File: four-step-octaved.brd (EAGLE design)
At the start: 93.7 x 43.2 mm, 36 parts, among them IC1 556, IC2 4017N, IC3 4040N, J1 BATTERY, J2 SPEAKER, U1 LM386N

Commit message: Routed
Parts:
- moved D2 0.63 mm to (5.08, 5.71)
- flipped C1 to the bottom
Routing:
- net GND: track 0.00 -> 250.5 mm
- net +9V: track 0.00 -> 132.8 mm
- net N$10: track 0.00 -> 79.7 mm
- net N$19: track 0.00 -> 78.7 mm
- net N$2: track 0.00 -> 66.8 mm
- net N$9: track 0.00 -> 63.4 mm
- net N$1: track 0.00 -> 57.8 mm
- net N$8: track 0.00 -> 52.4 mm
- net N$23: track 0.00 -> 38.9 mm
- net N$7: track 0.00 -> 38.1 mm
- net N$43: track 0.00 -> 29.6 mm
- net N$5: track 0.00 -> 28.6 mm
- net N$24: track 0.00 -> 21.4 mm
- net N$3: track 0.00 -> 18.8 mm
- net N$20: track 0.00 -> 18.5 mm
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
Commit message: Fix missing 556 pin10 on both schematics
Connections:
- net +9V: now also IC1.10
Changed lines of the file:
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@@
 <wire x1="35.49015" y1="35.49015" x2="31.2039" y2="39.7764" width="0.508" layer="1"/>
 <wire x1="15.4305" y1="38.9763" x2="15.24" y2="38.862" width="0.508" layer="1"/>
+<contactref element="IC1" pad="10"/>
+<wire x1="35.49015" y1="35.49015" x2="38.1" y2="27.94" width="0" layer="19" extent="1-1"/>
 </signal>
 <signal name="N$3" class="1">

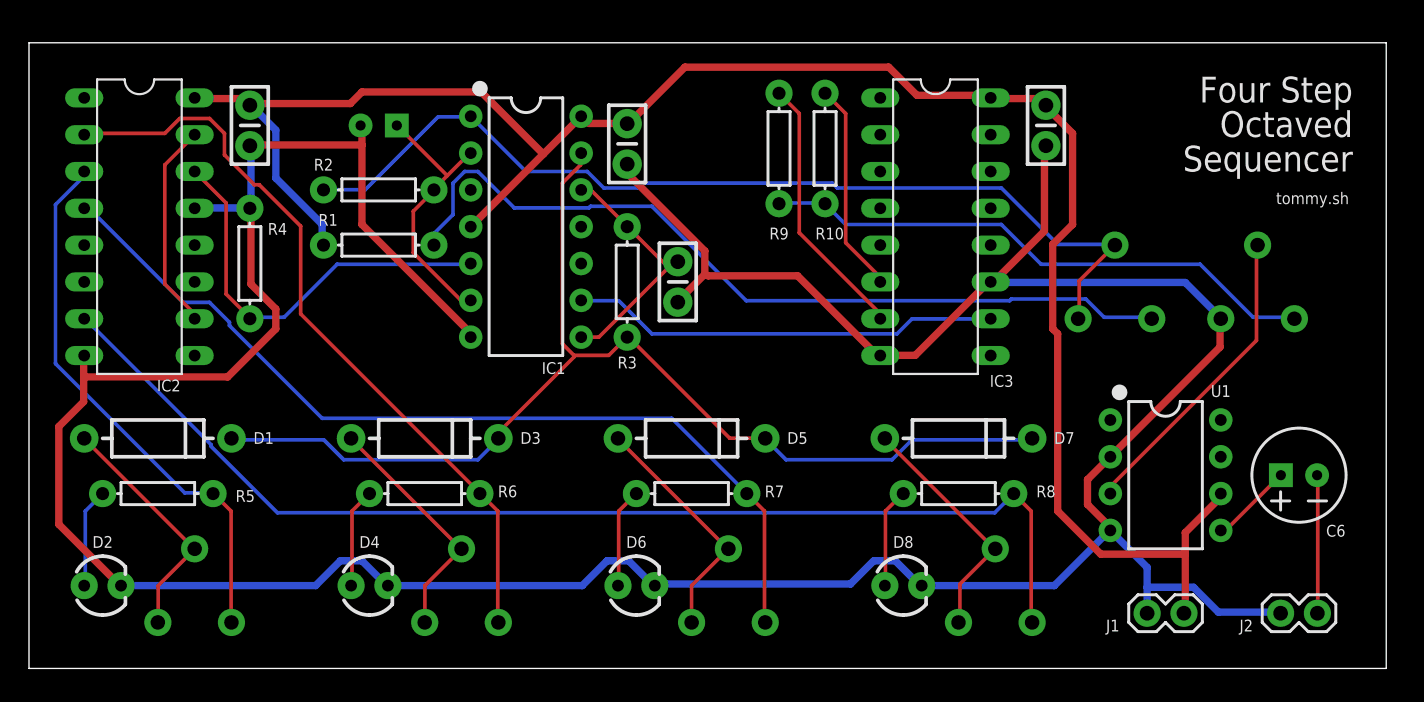
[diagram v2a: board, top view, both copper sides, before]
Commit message: Normalize versions
* Remove previous version
* Remove version filename prefix
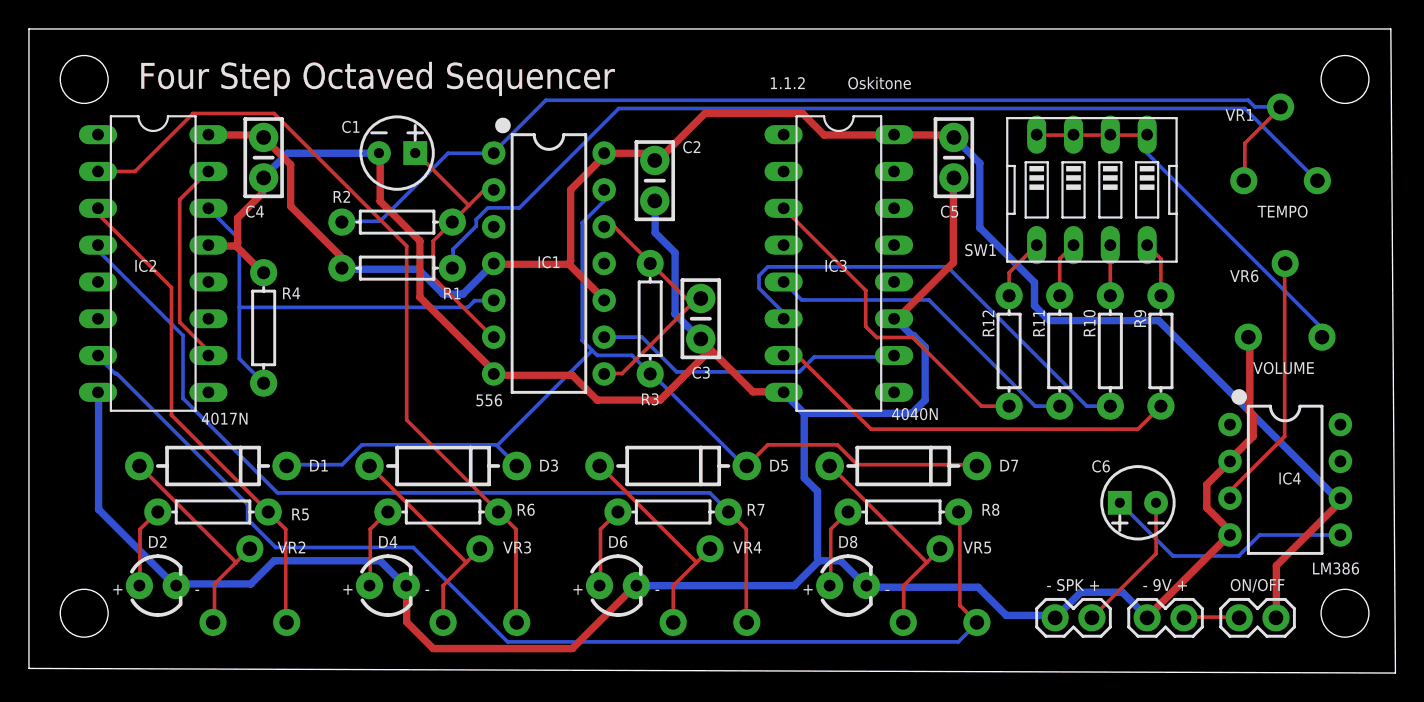
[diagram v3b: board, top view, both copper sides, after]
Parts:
- removed RV1, RV2, RV3, RV4, RV5: 50K, SparkFun-Retired:TRIM_POT
- removed U1: LM386N, SparkFun-IC-Amplifiers:DIP08
- added IC4: LM386, SparkFun-IC-Amplifiers:DIP08
- added J3: - SPK +, SparkFun-Connectors:1X02
- added R11, R12: 22K, SparkFun-Resistors:AXIAL-0.3
- added SW1: (no value), special:EDG-04
- added VR1, VR2, VR3, VR4, VR5: 50K, SparkFun-Retired:TRIM_POT
- C6: device SparkFun-Capacitors:CPOL-RADIAL-2.5MM-6.5MM -> SparkFun-Capacitors:CPOL-RADIAL-2.5MM-5MM
- J1: value BATTERY -> ON/OFF
- J2: value SPEAKER -> - 9V +
- moved R9 29.8 mm to (78.1, 21.9), turned to 270 degrees
- moved R10 24.1 mm to (74.6, 21.9), turned to 270 degrees
- moved C6 11.3 mm to (76.5, 11.4)
- moved J2 9.21 mm to (79.7, 3.49)
- moved IC3 7.13 mm to (55.9, 27.9)
- moved C5 6.73 mm to (63.8, 35.2)
- moved J1 6.36 mm to (86.0, 3.49)
- moved R4 4.55 mm to (16.2, 23.5)
- moved D7 4.26 mm to (60.3, 14.0)
- moved D1 4.26 mm to (12.7, 14.0)
- moved R8 4.02 mm to (60.3, 10.8)
- moved R5 4.02 mm to (12.7, 10.8)
- moved D8 3.81 mm to (56.5, 5.71)
- moved D2 3.81 mm to (8.89, 5.71)
- moved C2 3.18 mm to (43.2, 33.7)
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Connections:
- new net N$21: IC3.5, R11.P$2
- new net N$25: IC3.3, R12.P$2
- new net N$26: R11.P$1, SW1.6
- new net N$29: R10.P$1, SW1.7
- new net N$30: R9.P$1, SW1.8
- new net N$31: RV6.3, SW1.1, SW1.2, SW1.3, SW1.4
- new net N$32: J1.2, J2.1
- net +9V: now also IC4.6; no longer U1.6
- net GND: now also IC4.2, IC4.4, J3.2; no longer J1.2, U1.2, U1.4
- net N$1: now also VR1.3; no longer RV1.3
- net N$10: now also VR5.3; no longer RV5.3
- net N$11: now also VR2.1, VR2.2; no longer RV2.1, RV2.2
- net N$16: now also VR3.1, VR3.2; no longer RV3.1, RV3.2
- net N$17: now also VR4.1, VR4.2; no longer RV4.1, RV4.2
- net N$18: now also VR5.1, VR5.2; no longer RV5.1, RV5.2
- net N$2: now also VR1.1, VR1.2; no longer RV1.1, RV1.2
- net N$23: now also R12.P$1, SW1.5; no longer R10.P$1, R9.P$1, RV6.3
- net N$24: now also IC4.3; no longer U1.3
- net N$27: now also J3.1; no longer J2.1
- net N$28: now also IC4.5; no longer U1.5
- net N$7: now also VR2.3; no longer RV2.3
- net N$8: now also VR3.3; no longer RV3.3
- net N$9: now also VR4.3; no longer RV4.3
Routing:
- net N$23: track 38.9 -> 4.28 mm
- net N$31: track 0.00 -> 26.7 mm
- net N$25: track 0.00 -> 22.7 mm
- net N$21: track 0.00 -> 22.6 mm
- net GND: track 250.5 -> 229.7 mm
- net N$22: track 14.6 -> 32.2 mm
- net N$28: track 5.73 -> 17.3 mm
- net +9V: track 132.8 -> 121.6 mm
- net N$20: track 18.5 -> 28.8 mm
- net N$1: track 57.8 -> 67.3 mm
- net N$19: track 78.7 -> 69.6 mm
- net N$43: track 29.6 -> 21.5 mm
- net N$2: track 66.8 -> 74.6 mm
- net N$7: track 38.1 -> 34.0 mm
- net N$30: track 0.00 -> 3.89 mm
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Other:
- board size 93.7 x 43.2 mm -> 94.3 x 44.4 mm
- board text added: "+"
- board text added: "-"
- board text added: "1.1.2"
- board text added: "Oskitone"
- board text added: "VR1"
- board text added: "VR2"
- board text added: "VR3"
- board text added: "VR4"
- board text added: "VR5"
- board text added: "VR6"
- board text removed: "RV1"
- board text removed: "RV6"
- board text removed: "tommy.sh"

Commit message: Update mixing resistor values
to what is actually in kits!
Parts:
- R10, R11, R12, R9: value 22K -> 10k
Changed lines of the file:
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@@
 <?xml version="1.0" encoding="utf-8"?>
 <!DOCTYPE eagle SYSTEM "eagle.dtd">
-<eagle version="8.2.2">
+<eagle version="9.6.2">
 <drawing>
 <settings>
 <setting alwaysvectorfont="no"/>
+<setting keepoldvectorfont="yes"/>
 <setting verticaltext="up"/>
 </settings>
@@
 <param name="dpMaxLengthDifference" value="10mm"/>
 <param name="dpGapFactor" value="2.5"/>
-<param name="checkGrid" value="0"/>
 <param name="checkAngle" value="0"/>
 <param name="checkFont" value="1"/>
 <param name="checkRestrict" value="1"/>
+<param name="checkStop" value="0"/>
+<param name="checkValues" value="0"/>
+<param name="checkNames" value="1"/>
+<param name="checkWireStubs" value="1"/>
+<param name="checkPolygonWidth" value="0"/>
 <param name="useDiameter" value="13"/>
 <param name="maxErrors" value="50"/>
@@
 <attribute name="PROD_ID" value="RES-12182" x="25.4" y="27.6225" size="1.778" layer="27" display="off"/>
 </element>
-<element name="R10" library="SparkFun-Resistors" package="AXIAL-0.3" value="22K" x="74.6125" y="21.9075" smashed="yes" rot="R270">
+<element name="R10" library="SparkFun-Resistors" package="AXIAL-0.3" value="10k" x="74.6125" y="21.9075" smashed="yes" rot="R270">
 <attribute name="NAME" x="72.771" y="23.8125" size="0.8128" layer="25" font="vector" rot="R270" align="bottom-center"/>
 <attribute name="PROD_ID" value="RES-12182" x="74.6125" y="21.9075" size="1.778" layer="27" rot="R270" display="off"/>
@@
 <attribute name="PROD_ID" value="RES-12182" x="60.325" y="10.795" size="1.778" layer="27" display="off"/>
 </element>
-<element name="R9" library="SparkFun-Resistors" package="AXIAL-0.3" value="22K" x="78.105" y="21.9075" smashed="yes" rot="R270">
+<element name="R9" library="SparkFun-Resistors" package="AXIAL-0.3" value="10k" x="78.105" y="21.9075" smashed="yes" rot="R270">
 <attribute name="NAME" x="76.2635" y="24.13" size="0.8128" layer="25" font="vector" rot="R270" align="bottom-center"/>
 <attribute name="PROD_ID" value="RES-12182" x="78.105" y="21.9075" size="1.778" layer="27" rot="R270" display="off"/>
@@
 <attribute name="VALUE" x="90.17" y="7.3025" size="0.8128" layer="21" font="vector" rot="R180" align="bottom-center"/>
 </element>
-<element name="R11" library="SparkFun-Resistors" package="AXIAL-0.3" value="22K" x="71.12" y="21.9075" smashed="yes" rot="R270">
+<element name="R11" library="SparkFun-Resistors" package="AXIAL-0.3" value="10k" x="71.12" y="21.9075" smashed="yes" rot="R270">
 <attribute name="NAME" x="69.2785" y="23.8125" size="0.8128" layer="25" font="vector" rot="R270" align="bottom-center"/>
 <attribute name="PROD_ID" value="RES-12182" x="71.12" y="21.9075" size="1.778" layer="27" rot="R270" display="off"/>
 </element>
-<element name="R12" library="SparkFun-Resistors" package="AXIAL-0.3" value="22K" x="67.6275" y="21.9075" smashed="yes" rot="R270">
+<element name="R12" library="SparkFun-Resistors" package="AXIAL-0.3" value="10k" x="67.6275" y="21.9075" smashed="yes" rot="R270">
 <attribute name="NAME" x="66.6115" y="23.8125" size="0.8128" layer="25" font="vector" rot="R90" align="bottom-center"/>
 <attribute name="PROD_ID" value="RES-12182" x="67.6275" y="21.9075" size="1.778" layer="27" rot="R270" display="off"/>
@@
 </signal>
 </signals>
+<mfgpreviewcolors>
+<mfgpreviewcolor name="soldermaskcolor" color="0xC8008000"/>
+<mfgpreviewcolor name="silkscreencolor" color="0xFFFEFEFE"/>
+<mfgpreviewcolor name="backgroundcolor" color="0xFF282828"/>
+<mfgpreviewcolor name="coppercolor" color="0xFFFFBF00"/>
+<mfgpreviewcolor name="substratecolor" color="0xFF786E46"/>
+</mfgpreviewcolors>
 </board>
 </drawing>

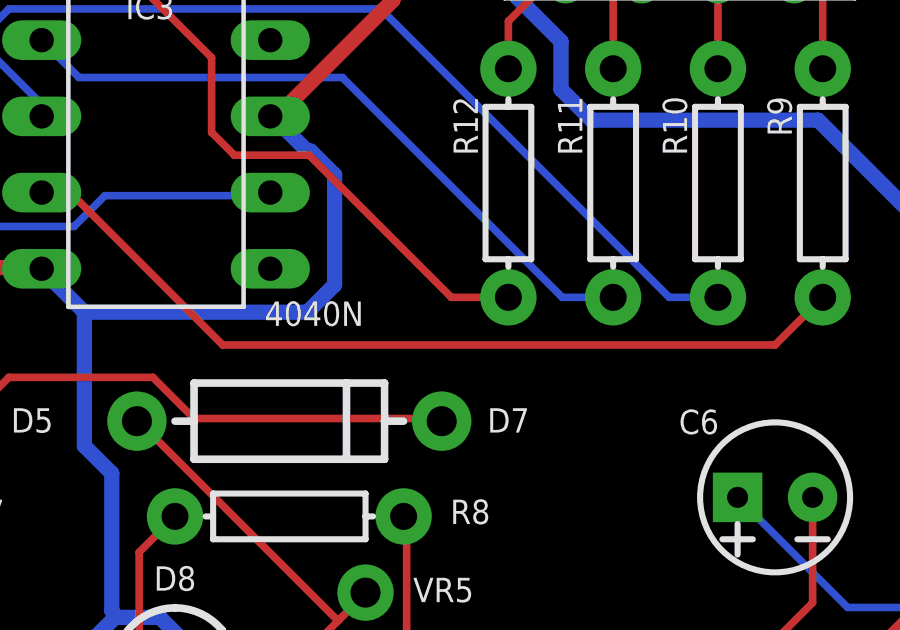
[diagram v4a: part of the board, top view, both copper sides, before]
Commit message: Denote alternate 4040 chip
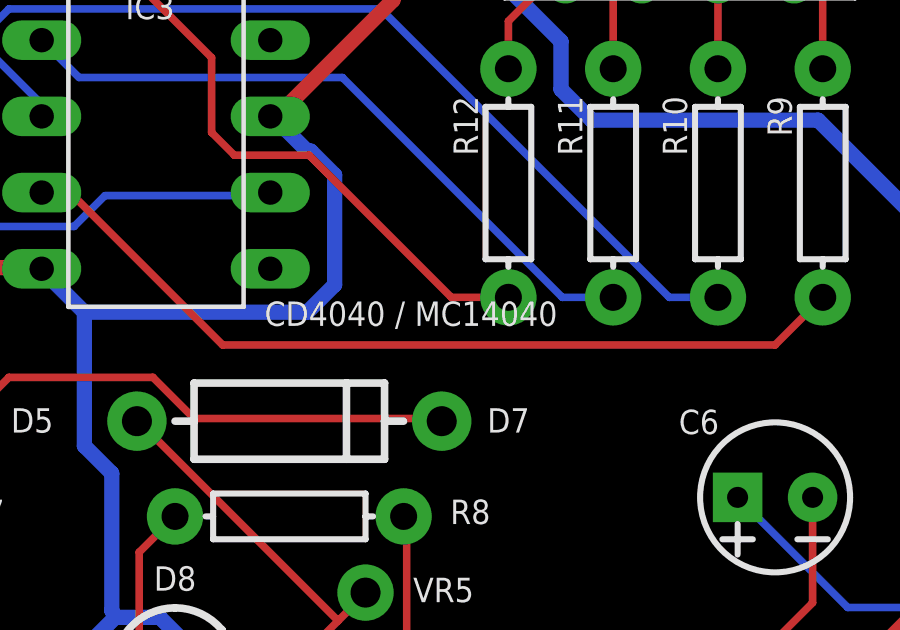
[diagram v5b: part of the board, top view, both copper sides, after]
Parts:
- IC3: value 4040N -> CD4040 / MC14040
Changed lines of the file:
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@@
 <attribute name="VALUE" x="11.8745" y="16.8275" size="0.8128" layer="21" font="vector"/>
 </element>
-<element name="IC3" library="40xx" package="DIL16" value="4040N" x="55.88" y="27.94" smashed="yes" rot="R270">
+<element name="IC3" library="40xx" package="DIL16" value="CD4040 / MC14040" x="55.88" y="27.94" smashed="yes" rot="R270">
 <attribute name="NAME" x="54.864" y="27.3685" size="0.8128" layer="25" font="vector"/>
 <attribute name="VALUE" x="59.4995" y="17.145" size="0.8128" layer="21" font="vector"/>

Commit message: Fix errant RV->VR name
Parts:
- renumbered RV6 to VR6
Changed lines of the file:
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@@
 <attribute name="PROD_ID" value="COM-00104" x="62.865" y="3.175" size="1.778" layer="27" rot="R90" display="off"/>
 </element>
-<element name="RV6" library="SparkFun-Retired" package="TRIM_POT" value="1K" x="86.6775" y="22.86" smashed="yes" rot="R90">
+<element name="VR6" library="SparkFun-Retired" package="TRIM_POT" value="1K" x="86.6775" y="22.86" smashed="yes" rot="R90">
 <attribute name="PROD_ID" value="COM-00104" x="86.6775" y="22.86" size="1.778" layer="27" rot="R90" display="off"/>
 </element>
@@
 </signal>
 <signal name="N$24" class="1">
-<contactref element="RV6" pad="1"/>
+<contactref element="VR6" pad="1"/>
 <contactref element="IC4" pad="3"/>
 <wire x1="82.8675" y1="12.2301" x2="82.8675" y2="11.7475" width="0.254" layer="1"/>
@@
 <contactref element="IC3" pad="8"/>
 <contactref element="IC3" pad="11"/>
-<contactref element="RV6" pad="2"/>
+<contactref element="VR6" pad="2"/>
 <contactref element="IC4" pad="2"/>
 <contactref element="IC4" pad="4"/>
@@
 <contactref element="SW1" pad="2"/>
 <contactref element="SW1" pad="3"/>
-<contactref element="RV6" pad="3"/>
+<contactref element="VR6" pad="3"/>
 <wire x1="72.009" y1="36.8046" x2="69.6087" y2="36.8046" width="0.254" layer="1"/>
 <wire x1="69.6087" y1="36.8046" x2="69.5325" y2="36.83" width="0.254" layer="1"/>
